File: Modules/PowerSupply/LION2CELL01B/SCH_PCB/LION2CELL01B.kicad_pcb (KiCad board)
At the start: 2 copper layers, 81.3 x 61 mm, 93 parts, among them J1 JUMP_4X2, J10 JUMP_2x1, J11 JUMP_2x1, J12 JUMP_2x1, J13 JUMP_4X2, J2 JUMP_2x1, J3 JUMP_2x1, J4 JUMP_2x1, J5 JUMP_2x1, J6 JUMP_2x1, J7 JUMP_4X2, J8 CONN1_1, J9 CONN1_1, P1 _, P2 _, P3 _, P4 _, Q1 IRLML6244, Q2 MMBF170LT1G, Q3 MMBF170LT1G, Q4 BSS83P, SW1 SW_PUSH, U1 BQ29209, U2 BQ24103, U3 BQ34Z100, U4 SN74HC164D

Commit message: 
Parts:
- added J14: JUMP_2x1, Mlab_Pin_Headers:Straight_1x02, F.Cu at (70.5, -55.6)
- C10: value 47uF -> 100uF; footprint Mlab_C:TantalC_SizeC_Reflow -> Mlab_C:TantalC_SizeD_Reflow
- moved J12 262.0 mm to (67.9, -55.6)
- moved J7 252.1 mm to (35.6, -5.08), turned to 90 degrees
- moved J10 216.9 mm to (62.9, -55.6)
- moved J11 209.2 mm to (65.4, -55.6)
- moved Q4 47.1 mm to (50.3, -33.0), turned to 270 degrees
- moved R23 46.9 mm to (46.5, -32.9)
- moved C17 46.6 mm to (44.2, -32.9)
- moved R24 46.2 mm to (48.1, -36.2)
- moved R26 44.9 mm to (54.2, -33.5), turned to 0 degrees
- moved R25 39.9 mm to (55.1, -35.7), turned to 0 degrees
- moved Q3 34.9 mm to (54.4, -30.6), turned to 180 degrees
- moved D2 15.7 mm to (18.5, -38.1), turned to 270 degrees
- moved D5 12.2 mm to (34.9, -55.9), turned to 90 degrees
- moved R8 11.6 mm to (32.4, -52.5), turned to 90 degrees
- moved R28 9.96 mm to (46.9, -9.65)
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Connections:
- net /BAT- renamed /BAT-MIDPOINT
- net /BATERY+ renamed /BATTERY+
- net /BATERY- renamed /BATTERY-
- net Net-(J10-Pad1) renamed /SDA
- net Net-(J11-Pad1) renamed /SCL
- net Net-(J12-Pad1) renamed /HDQ
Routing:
- net GND: track 0.00 -> 106.0 mm, vias 0 -> 24
- net /REGIN: track 0.00 -> 69.3 mm
- net /STAT1: track 0.50 -> 53.3 mm, vias 0 -> 2
- net /BATTERY+: track 11.5 -> 62.4 mm, vias 0 -> 2
- net /PG: track 0.00 -> 38.6 mm, vias 0 -> 2
- net Net-(Q3-PadG): track 0.00 -> 38.3 mm
- net /SDA: track 0.00 -> 37.9 mm
- net /SCL: track 0.00 -> 37.7 mm
- net /HDQ: track 0.00 -> 37.6 mm
- net /CMODE: track 0.00 -> 35.0 mm, vias 0 -> 1
- net /CE: track 0.00 -> 29.6 mm, vias 0 -> 1
- net Net-(C14-Pad1): track 0.00 -> 27.8 mm, vias 0 -> 2
- net Net-(C17-Pad1): track 0.00 -> 20.6 mm
- net Net-(D4-Pad2): track 0.00 -> 20.2 mm, vias 0 -> 2
- net /P1: track 0.00 -> 19.3 mm, vias 0 -> 2
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- added copper zone on B.Cu, net /BAT+
- added copper zone on B.Cu, net /BAT-MIDPOINT
- added copper zone on F.Cu, net /BAT-MIDPOINT
- added copper zone on B.Cu, net /BATTERY+
- added copper zone on B.Cu, net /BATTERY-
- added copper zone on B.Cu, net /REGIN
- added copper zone on B.Cu, net GND
- added copper zone on F.Cu, net GND
- added copper zone on B.Cu, net Net-(C10-Pad1)
- added copper zone on B.Cu, net Net-(C2-Pad1)
- added copper zone on B.Cu, net Net-(L1-Pad1)
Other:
- net class Default: via_dia 0.889 -> 0.4; via_drill 0.635 -> 0.3
- rule via_min_drill: 0.508 -> 0.3
- rule via_min_size: 0.889 -> 0.3
- board text added: "0% ----100%"
- board text added: "CHARGE"
- board text added: "DONE"
- board text added: "ON"

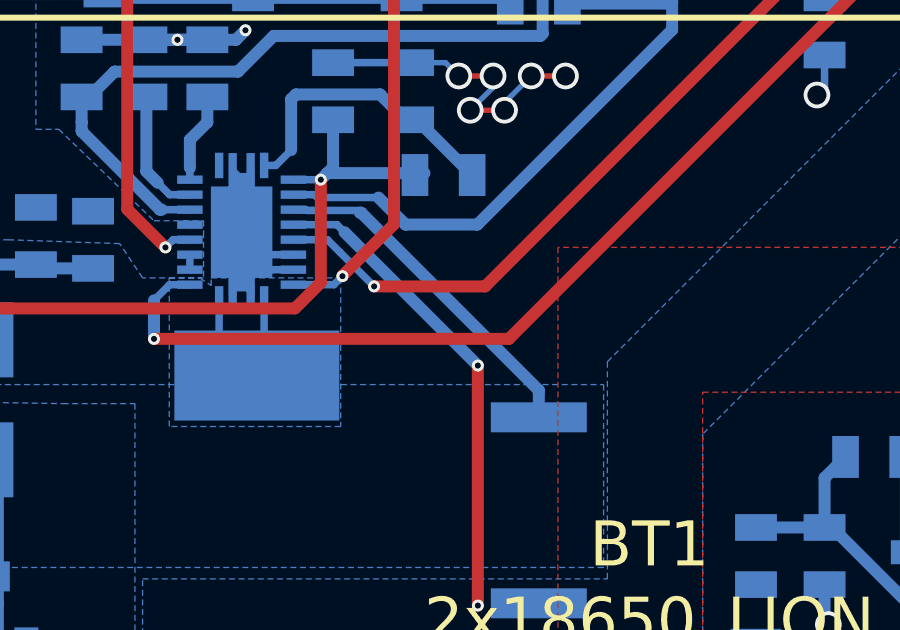
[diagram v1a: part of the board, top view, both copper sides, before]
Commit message: 
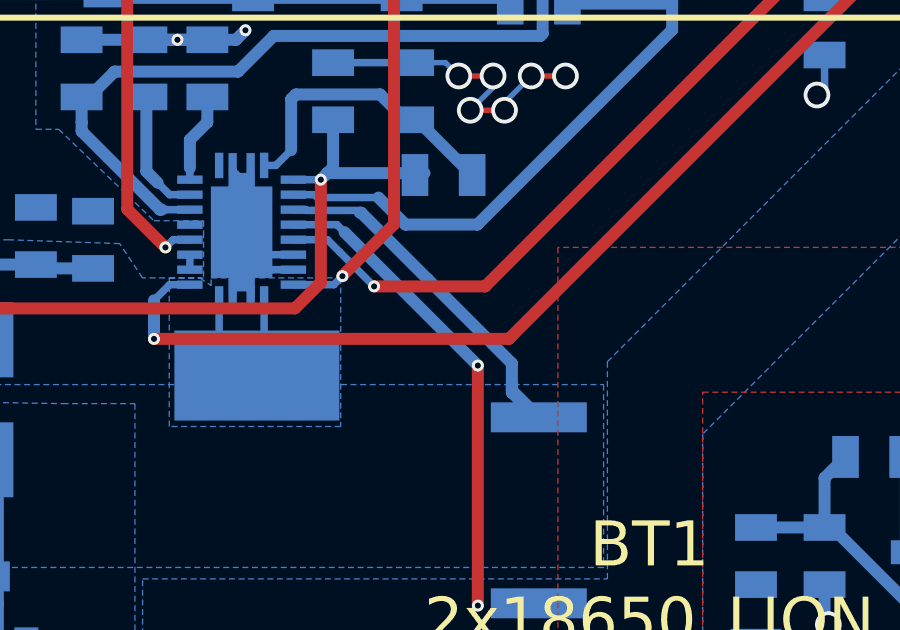
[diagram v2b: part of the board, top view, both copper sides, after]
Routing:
- net /BATTERY+: track 62.4 -> 63.9 mm

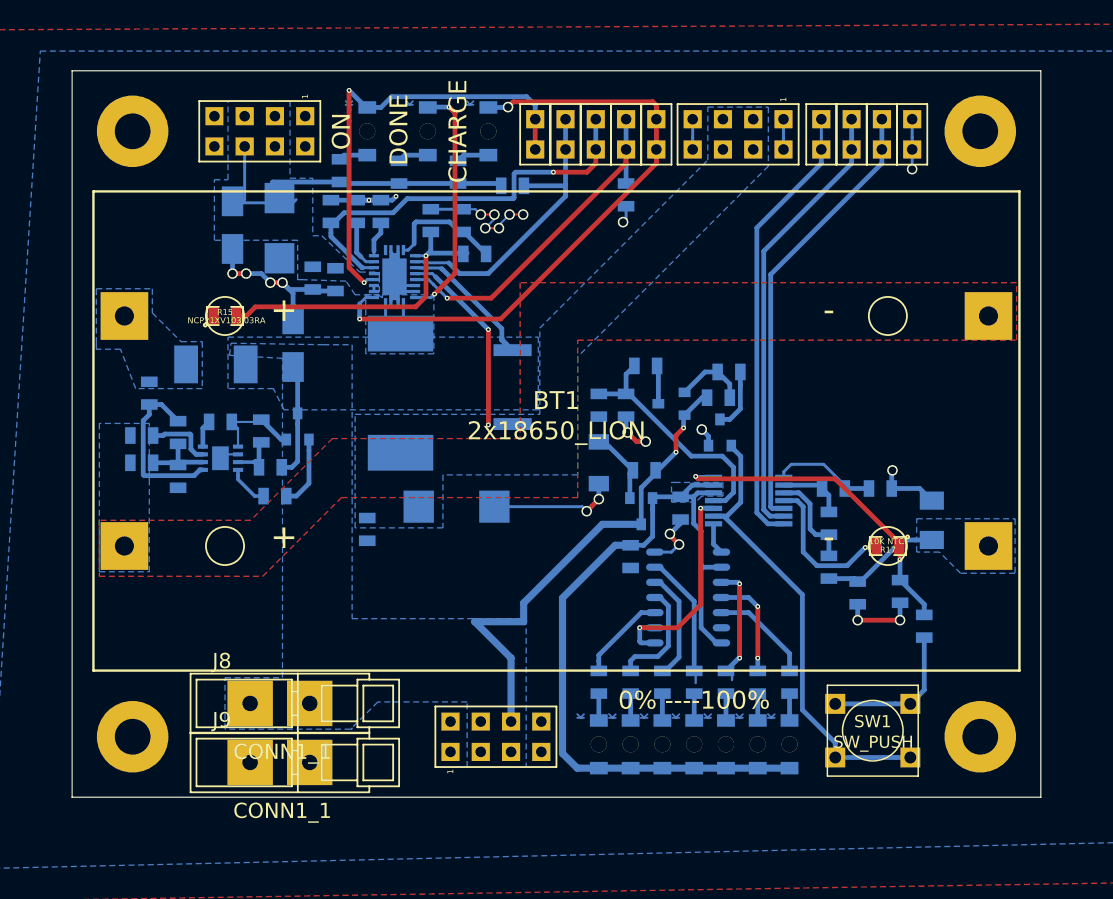
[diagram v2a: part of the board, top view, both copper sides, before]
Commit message: 
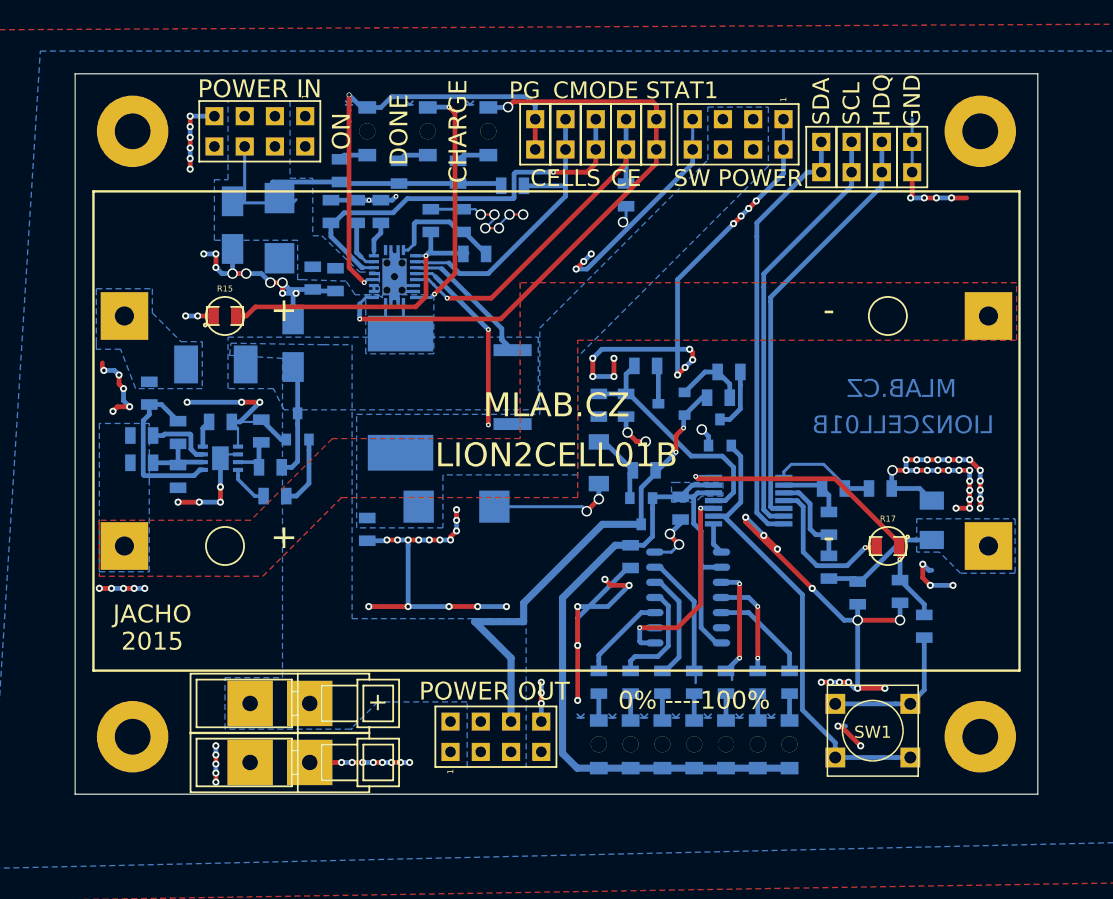
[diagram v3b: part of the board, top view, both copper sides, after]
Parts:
- moved J10 1.91 mm to (62.9, -53.7)
- moved J11 1.91 mm to (65.4, -53.7)
- moved J12 1.91 mm to (67.9, -53.7)
- moved J14 1.91 mm to (70.5, -53.7)
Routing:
- net GND: track 106.0 -> 314.2 mm, vias 24 -> 127
- net (no net): track 0.00 -> 22.0 mm, vias 0 -> 20
- net /SCL: track 37.7 -> 34.4 mm
- net /HDQ: track 37.6 -> 34.3 mm
- net /SDA: track 37.9 -> 35.3 mm
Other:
- board size 81.3 x 61 mm -> 80.8 x 60.5 mm
- board text added: "+"
- board text added: "2015"
- board text added: "CE"
- board text added: "CELLS"
- board text added: "CMODE"
- board text added: "GND"
- board text added: "HDQ"
- board text added: "JACHO"
- board text added: "LION2CELL01B"
- board text added: "MLAB.CZ"
- board text added: "PG"
- board text added: "POWER IN"
- board text added: "POWER OUT"
- board text added: "SCL"
- board text added: "SDA"
- board text added: "STAT1"
- board text added: "SW POWER"

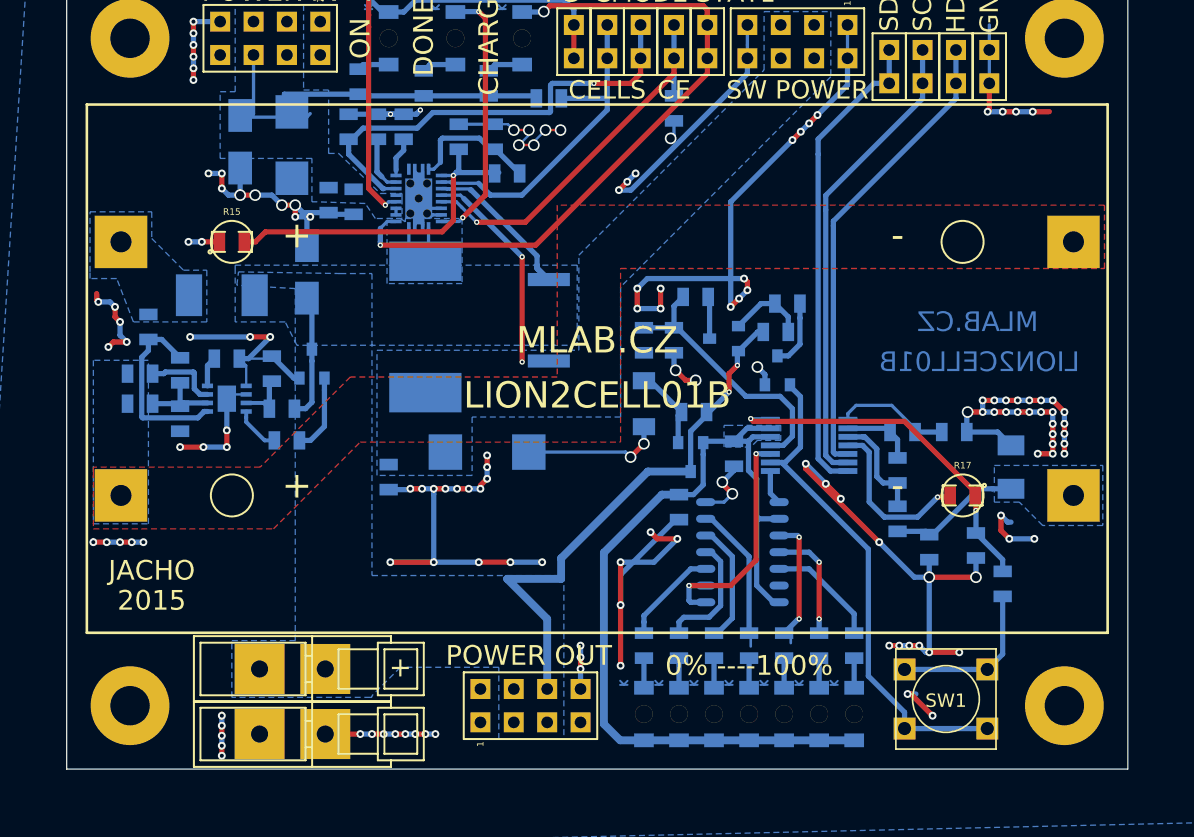
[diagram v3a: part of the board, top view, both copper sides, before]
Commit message: 
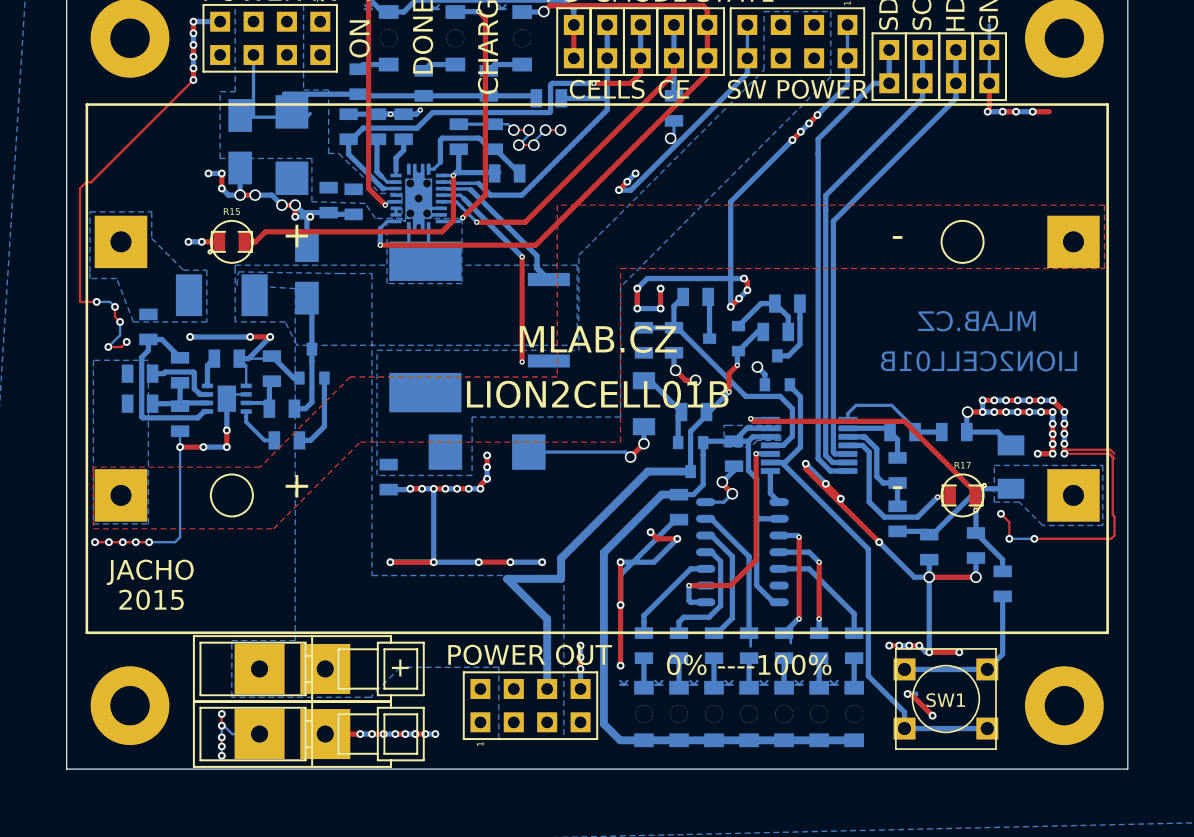
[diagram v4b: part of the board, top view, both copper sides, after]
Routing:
- net GND: track 314.2 -> 389.4 mm, vias 127 -> 145
- net (no net): track 22.0 -> 3.22 mm, vias 20 -> 2

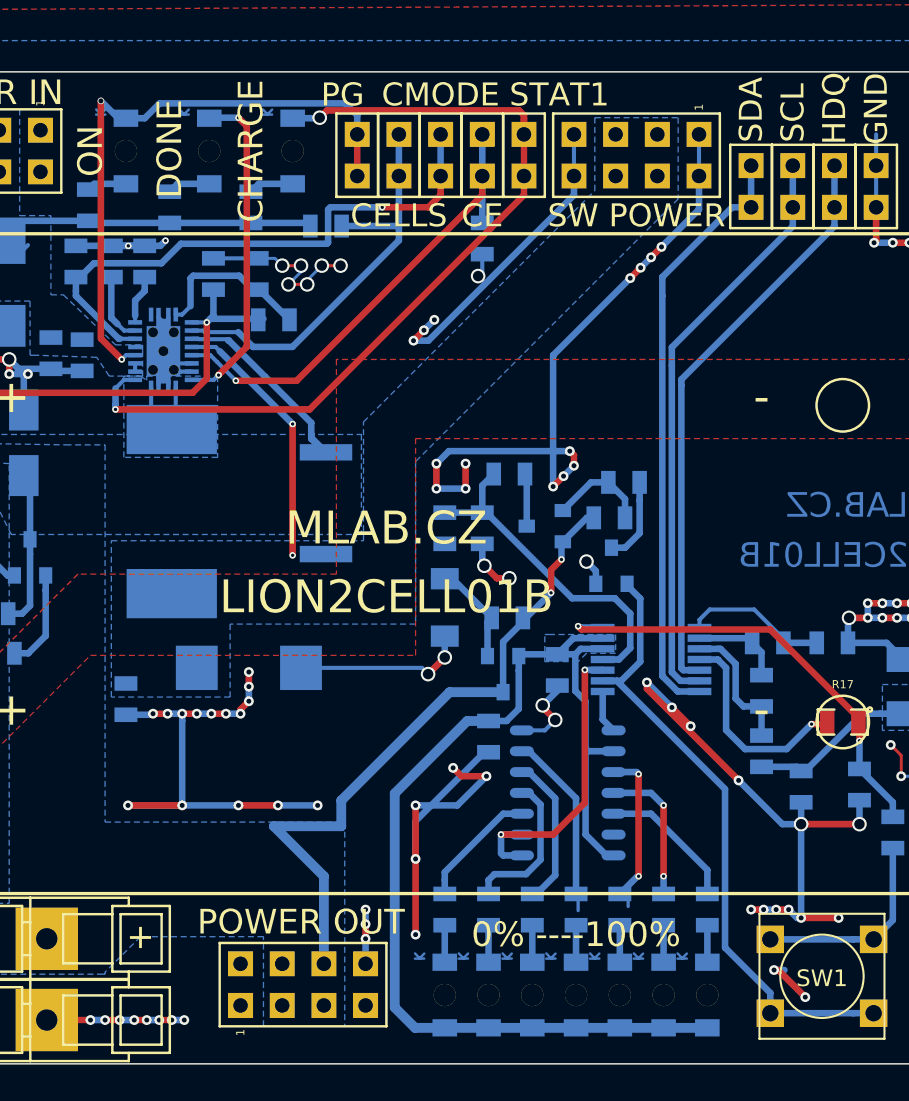
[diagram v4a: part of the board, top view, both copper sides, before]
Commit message: 
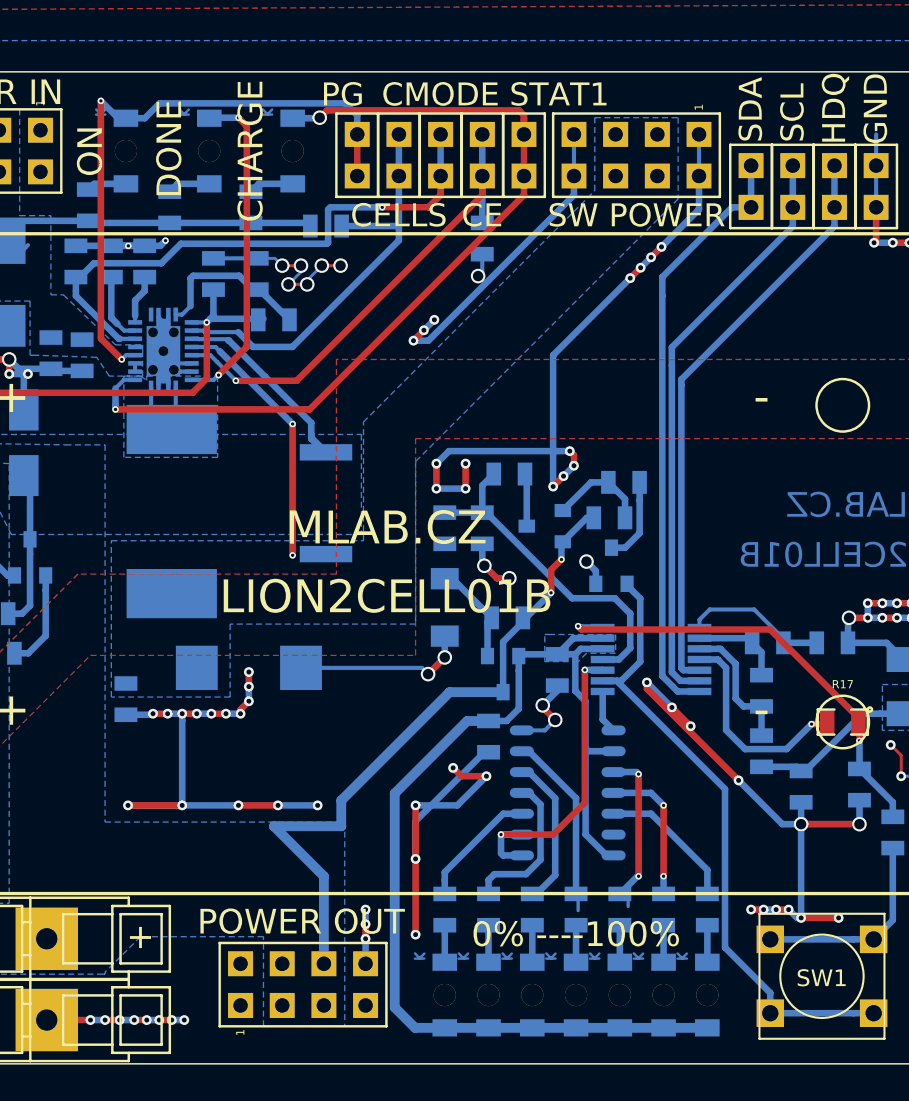
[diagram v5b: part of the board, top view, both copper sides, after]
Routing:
- net (no net): track 3.22 -> 0.00 mm, vias 2 -> 0
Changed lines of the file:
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@@
     (links 207)
     (no_connects 0)
-    (area 0.203999 -60.756001 81.076001 -0.203999)
+    (area -10.541 -64.897 93.345001 8.763001)
     (thickness 1.6)
     (drawings 27)
-    (tracks 813)
+    (tracks 808)
     (zones 0)
     (modules 94)
@@
   (gr_line (start 81.026 -0.254) (end 81.026 -60.706) (angle 90) (layer Edge.Cuts) (width 0.1))
   (gr_line (start 0.254 -0.254) (end 81.026 -0.254) (angle 90) (layer Edge.Cuts) (width 0.1))
-  (via (at 64.262 -5.969) (size 0.6) (layers F.Cu B.Cu) (net 0))
-  (segment (start 64.897 -5.969) (end 64.262 -5.969) (width 0.4) (layer B.Cu) (net 0))
-  (via (at 66.167 -4.318) (size 0.6) (layers F.Cu B.Cu) (net 0))
-  (segment (start 64.516 -5.969) (end 66.167 -4.318) (width 0.4) (layer F.Cu) (net 0))
-  (segment (start 64.262 -5.969) (end 64.516 -5.969) (width 0.4) (layer F.Cu) (net 0))
   (segment (start 8.89 -27.8765) (end 8.89 -29.6545) (width 0.4) (layer B.Cu) (net 2))
   (segment (start 6.7945 -28.067) (end 8.6995 -28.067) (width 0.4) (layer B.Cu) (net 2))
@@
   (via (at 24.511 -43.18) (size 0.4) (layers F.Cu B.Cu) (net 17))
   (segment (start 38.862 -54.356) (end 38.862 -56.896) (width 0.4) (layer F.Cu) (net 17))
-  (via (at 23.241 -58.934168) (size 0.4) (drill 0.3) (layers F.Cu B.Cu) (net 17))
+  (via (at 23.241 -58.934168) (size 0.4) (layers F.Cu B.Cu) (net 17))
   (segment (start 24.295168 -57.88) (end 23.241 -58.934168) (width 0.4) (layer B.Cu) (net 17))
   (segment (start 24.765 -57.88) (end 24.295168 -57.88) (width 0.4) (layer B.Cu) (net 17))
